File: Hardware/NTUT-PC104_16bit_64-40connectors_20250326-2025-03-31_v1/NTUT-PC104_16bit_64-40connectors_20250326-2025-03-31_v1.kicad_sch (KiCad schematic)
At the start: 41 parts, among them J10 Conn_02x26_Odd_Even, J12 Conn_02x04_Odd_Even, J13 Conn_02x04_Odd_Even, J14 Conn_02x04_Odd_Even, J15 Conn_02x04_Odd_Even, J16 Conn_02x04_Odd_Even, J17 Conn_02x04_Odd_Even, J18 Conn_02x04_Odd_Even, J7 Conn_02x04_Odd_Even, J8 Conn_02x26_Odd_Even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

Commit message: Copper Pour
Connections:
- net 5V_ADCS: now also J15.2 (Pin_2), J15.4 (Pin_4), J15.6 (Pin_6), J15.8 (Pin_8); no longer J15.1 (Pin_1), J15.3 (Pin_3), J15.5 (Pin_5), J15.7 (Pin_7)
- net 5V_ADCS_1.2W: now also J15.1 (Pin_1), J15.3 (Pin_3), J15.5 (Pin_5), J15.7 (Pin_7); no longer J15.2 (Pin_2), J15.4 (Pin_4), J15.6 (Pin_6), J15.8 (Pin_8)
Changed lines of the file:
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@@
 		)
 	)
-	(label "5V_ADCS_1.2W"
+	(label "5V_ADCS"
 		(at 556.26 304.8 0)
 		(effects
@@
 		)
 	)
-	(label "5V_ADCS"
+	(label "5V_ADCS_1.2W"
 		(at 521.97 304.8 0)
 		(effects

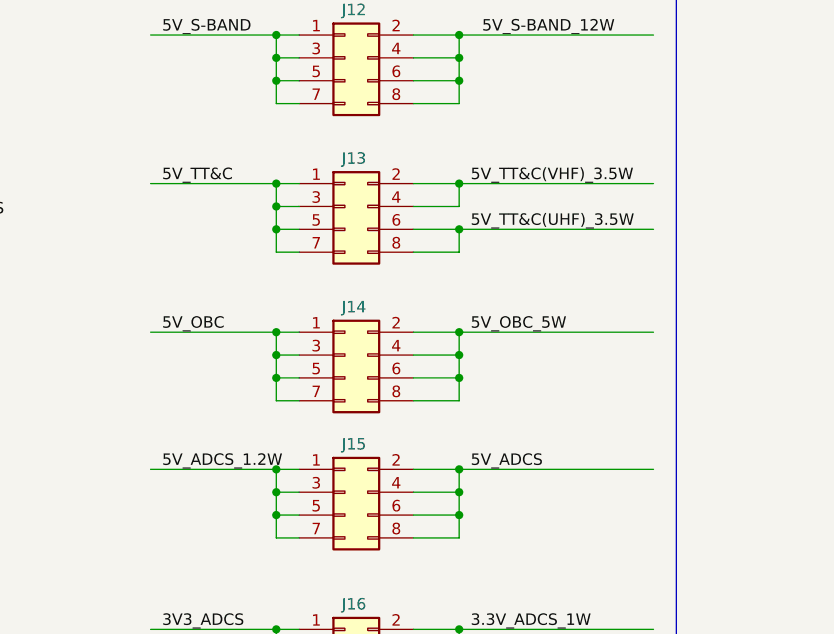
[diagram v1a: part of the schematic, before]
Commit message: Modify the pins below the banana socket
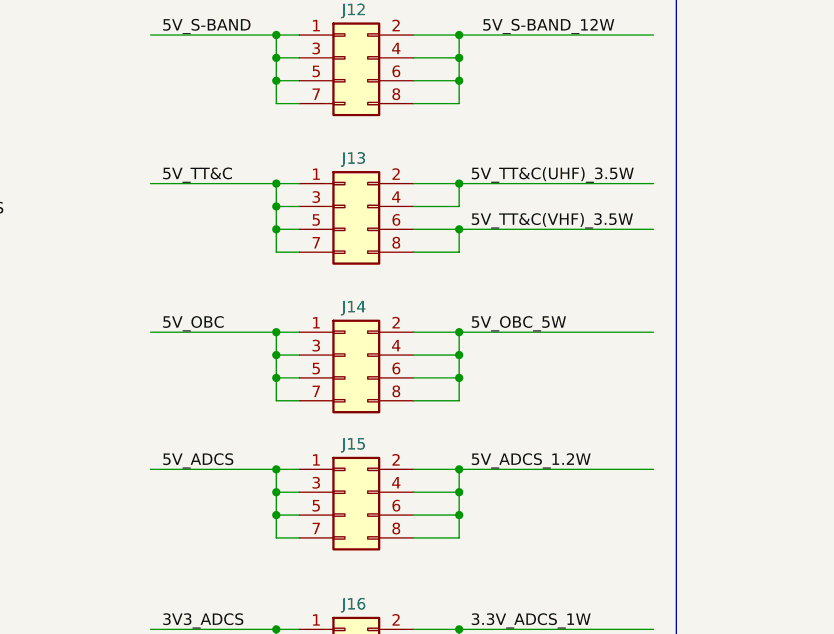
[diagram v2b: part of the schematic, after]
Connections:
- net 5V_ADCS: now also J15.1 (Pin_1), J15.3 (Pin_3), J15.5 (Pin_5), J15.7 (Pin_7); no longer J15.2 (Pin_2), J15.4 (Pin_4), J15.6 (Pin_6), J15.8 (Pin_8)
- net 5V_ADCS_1.2W: now also J15.2 (Pin_2), J15.4 (Pin_4), J15.6 (Pin_6), J15.8 (Pin_8); no longer J15.1 (Pin_1), J15.3 (Pin_3), J15.5 (Pin_5), J15.7 (Pin_7)
- net 5V_TT&C(UHF)_3.5W: now also J13.2 (Pin_2), J13.4 (Pin_4); no longer J13.6 (Pin_6), J13.8 (Pin_8)
- net 5V_TT&C(VHF)_3.5W: now also J13.6 (Pin_6), J13.8 (Pin_8); no longer J13.2 (Pin_2), J13.4 (Pin_4)
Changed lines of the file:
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@@
 		)
 	)
-	(label "5V_ADCS"
+	(label "5V_ADCS_1.2W"
 		(at 556.26 304.8 0)
 		(effects
@@
 		)
 	)
-	(label "5V_TT&C(VHF)_3.5W"
+	(label "5V_TT&C(UHF)_3.5W"
 		(at 556.26 273.05 0)
 		(effects
@@
 		)
 	)
-	(label "5V_ADCS_1.2W"
+	(label "5V_ADCS"
 		(at 521.97 304.8 0)
 		(effects
@@
 		)
 	)
-	(label "5V_TT&C(UHF)_3.5W"
+	(label "5V_TT&C(VHF)_3.5W"
 		(at 556.26 278.13 0)
 		(effects
